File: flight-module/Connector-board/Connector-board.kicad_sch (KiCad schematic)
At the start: 15 parts, among them J1 DB9_Female, J2 Stack_Shape, J3 DB9_Female, J4 DB15_Female, J5 DB25_Receptacle

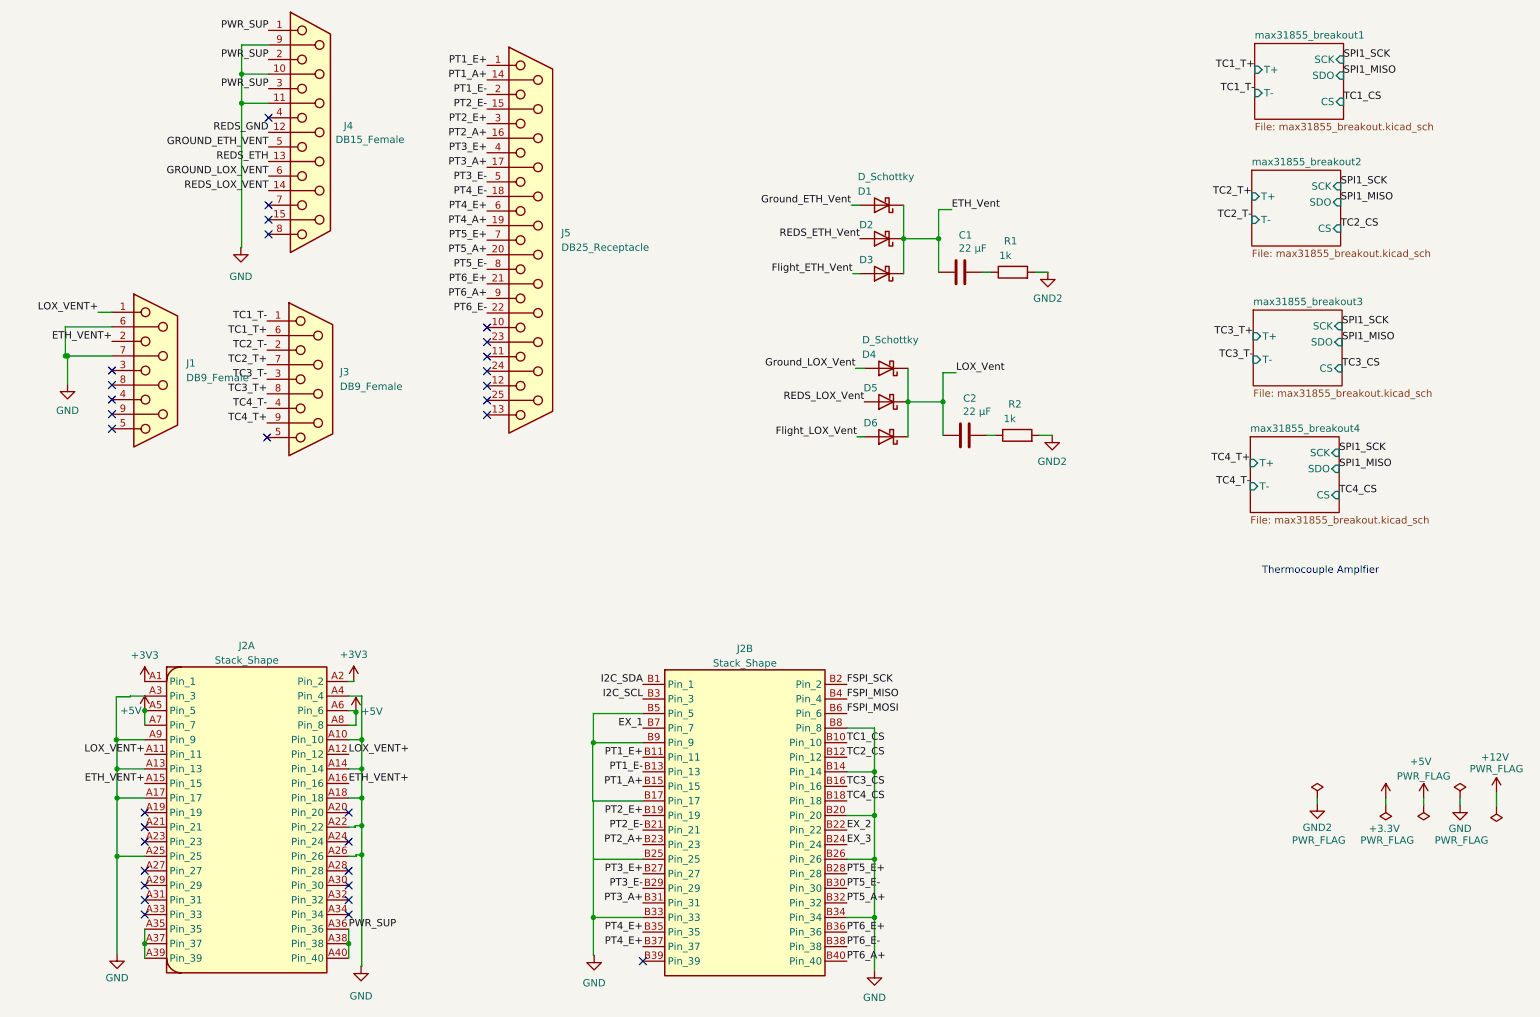
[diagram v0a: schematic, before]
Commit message: Edited the connector board to make sense
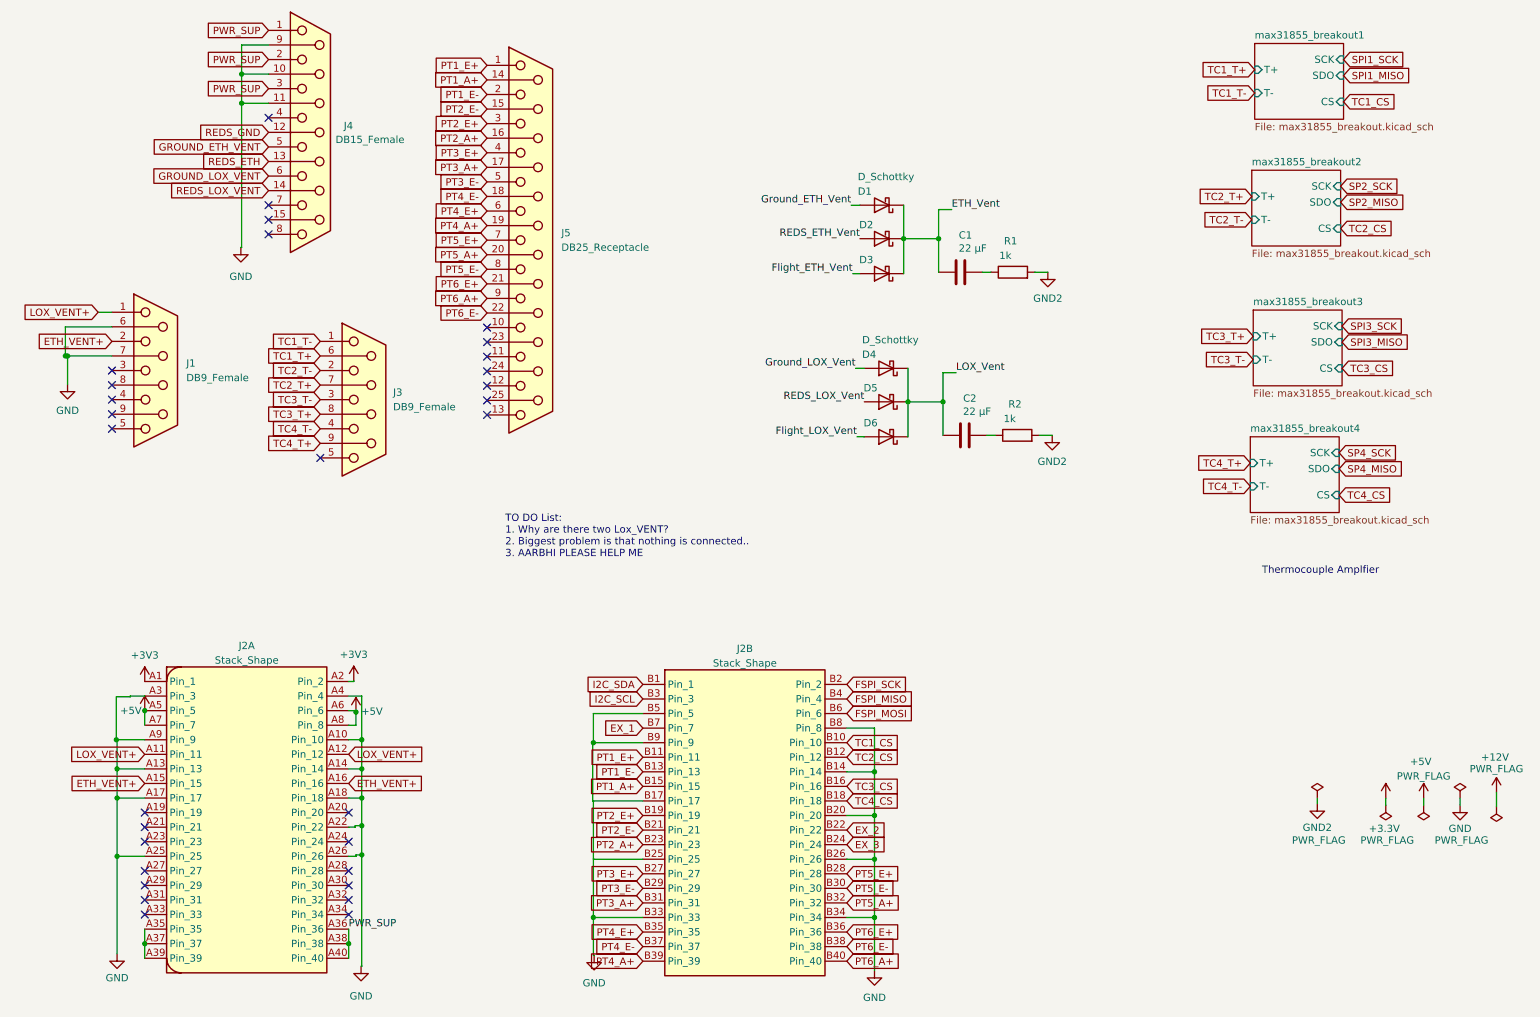
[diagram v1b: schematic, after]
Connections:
- net PT4_A+: now also J2.B39 (Pin_39)
- net PT4_E+: no longer J2.B37 (Pin_37)
- net PT4_E-: now also J2.B37 (Pin_37)
- no-connect marks 31 -> 30
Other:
- note added: "TO DO List: 1. Why are there two Lox_VENT? 2. Biggest problem is that nothing is connected.. 3. AARBHI PLEASE HELP ME"
- moved on the sheet: J3
